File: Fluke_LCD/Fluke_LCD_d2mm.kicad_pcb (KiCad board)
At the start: 2 copper layers, 64.3 x 34 mm, 65 parts, among them J1 Conn_01x23

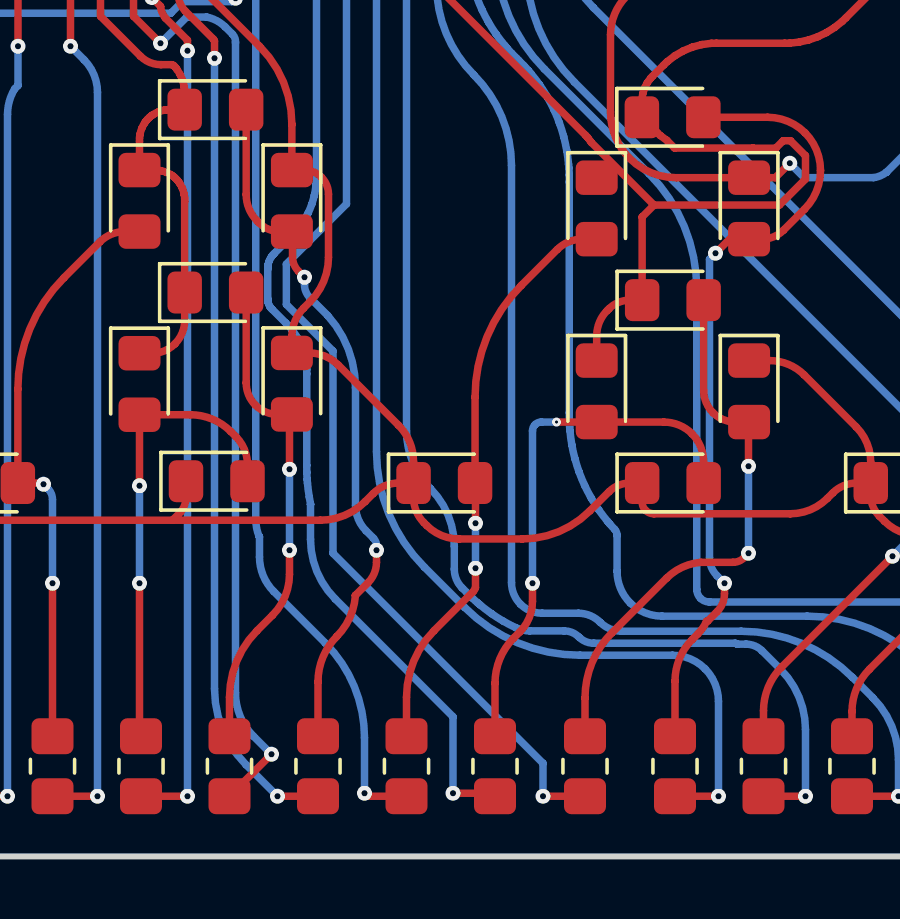
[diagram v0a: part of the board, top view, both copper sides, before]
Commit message: Edit via sizes
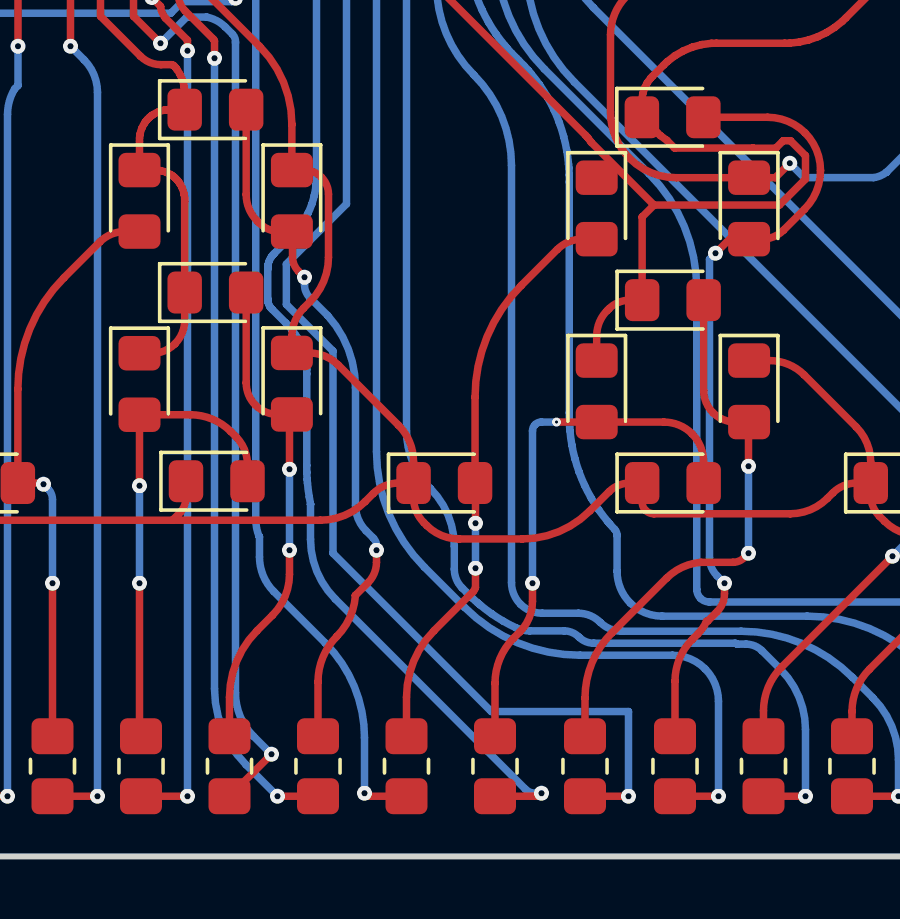
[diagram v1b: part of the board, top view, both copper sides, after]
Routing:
- net Net-(J1-Pin_9): track 36.8 -> 40.7 mm
- net Net-(J1-Pin_10): track 35.1 -> 36.7 mm

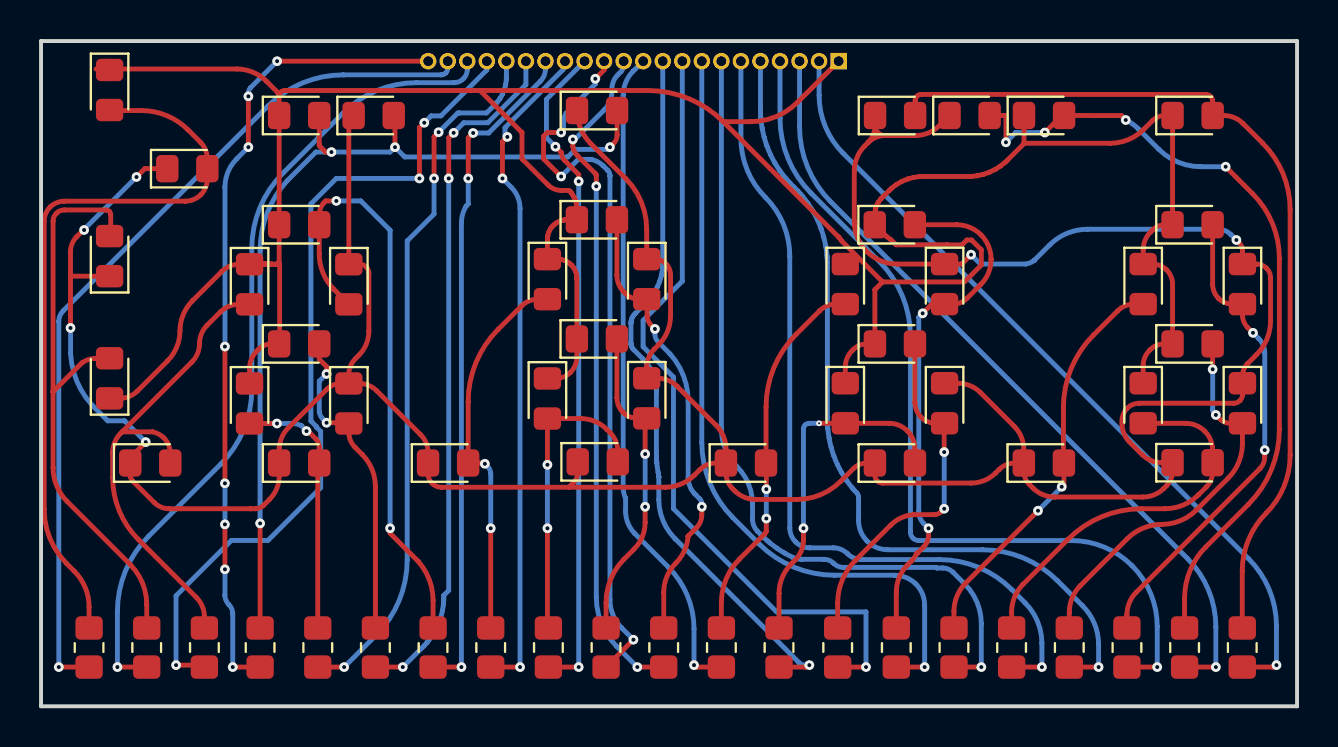
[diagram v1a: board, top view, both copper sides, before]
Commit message: Add Teardrops/Clean Traces on Fluke_LCD_d2mm
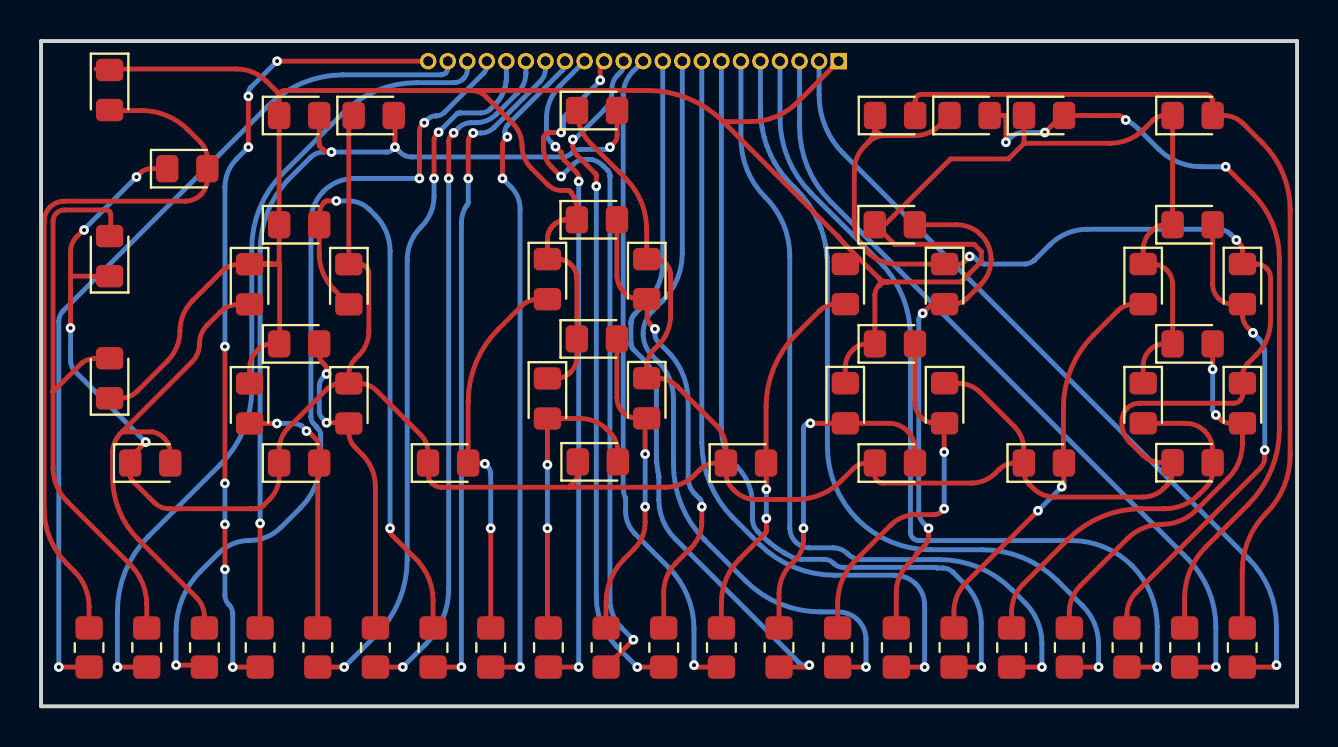
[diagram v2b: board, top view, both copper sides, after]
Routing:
- net Net-(J1-Pin_9): track 40.7 -> 39.0 mm
- net Net-(J1-Pin_19): track 43.3 -> 42.3 mm
- net /TopGround: track 154.8 -> 154.1 mm
